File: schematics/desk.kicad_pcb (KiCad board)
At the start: 2 copper layers, 194 x 185 mm, 34 parts, among them K1 energized = UP (raises desk), K2 energized = DOWN (lowers desk), Q1 IRLZ44N, Q2 2N7000, Q3 2N7000, Q4 BC337, Q5 BC327, U1 LM2596HV 29V-5V, U2 PinSocket_1x22_P2.54mm_Vertic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, U3 74HC123 250ms, U5 ACS724xLCTR-05AB, U6 74HC08

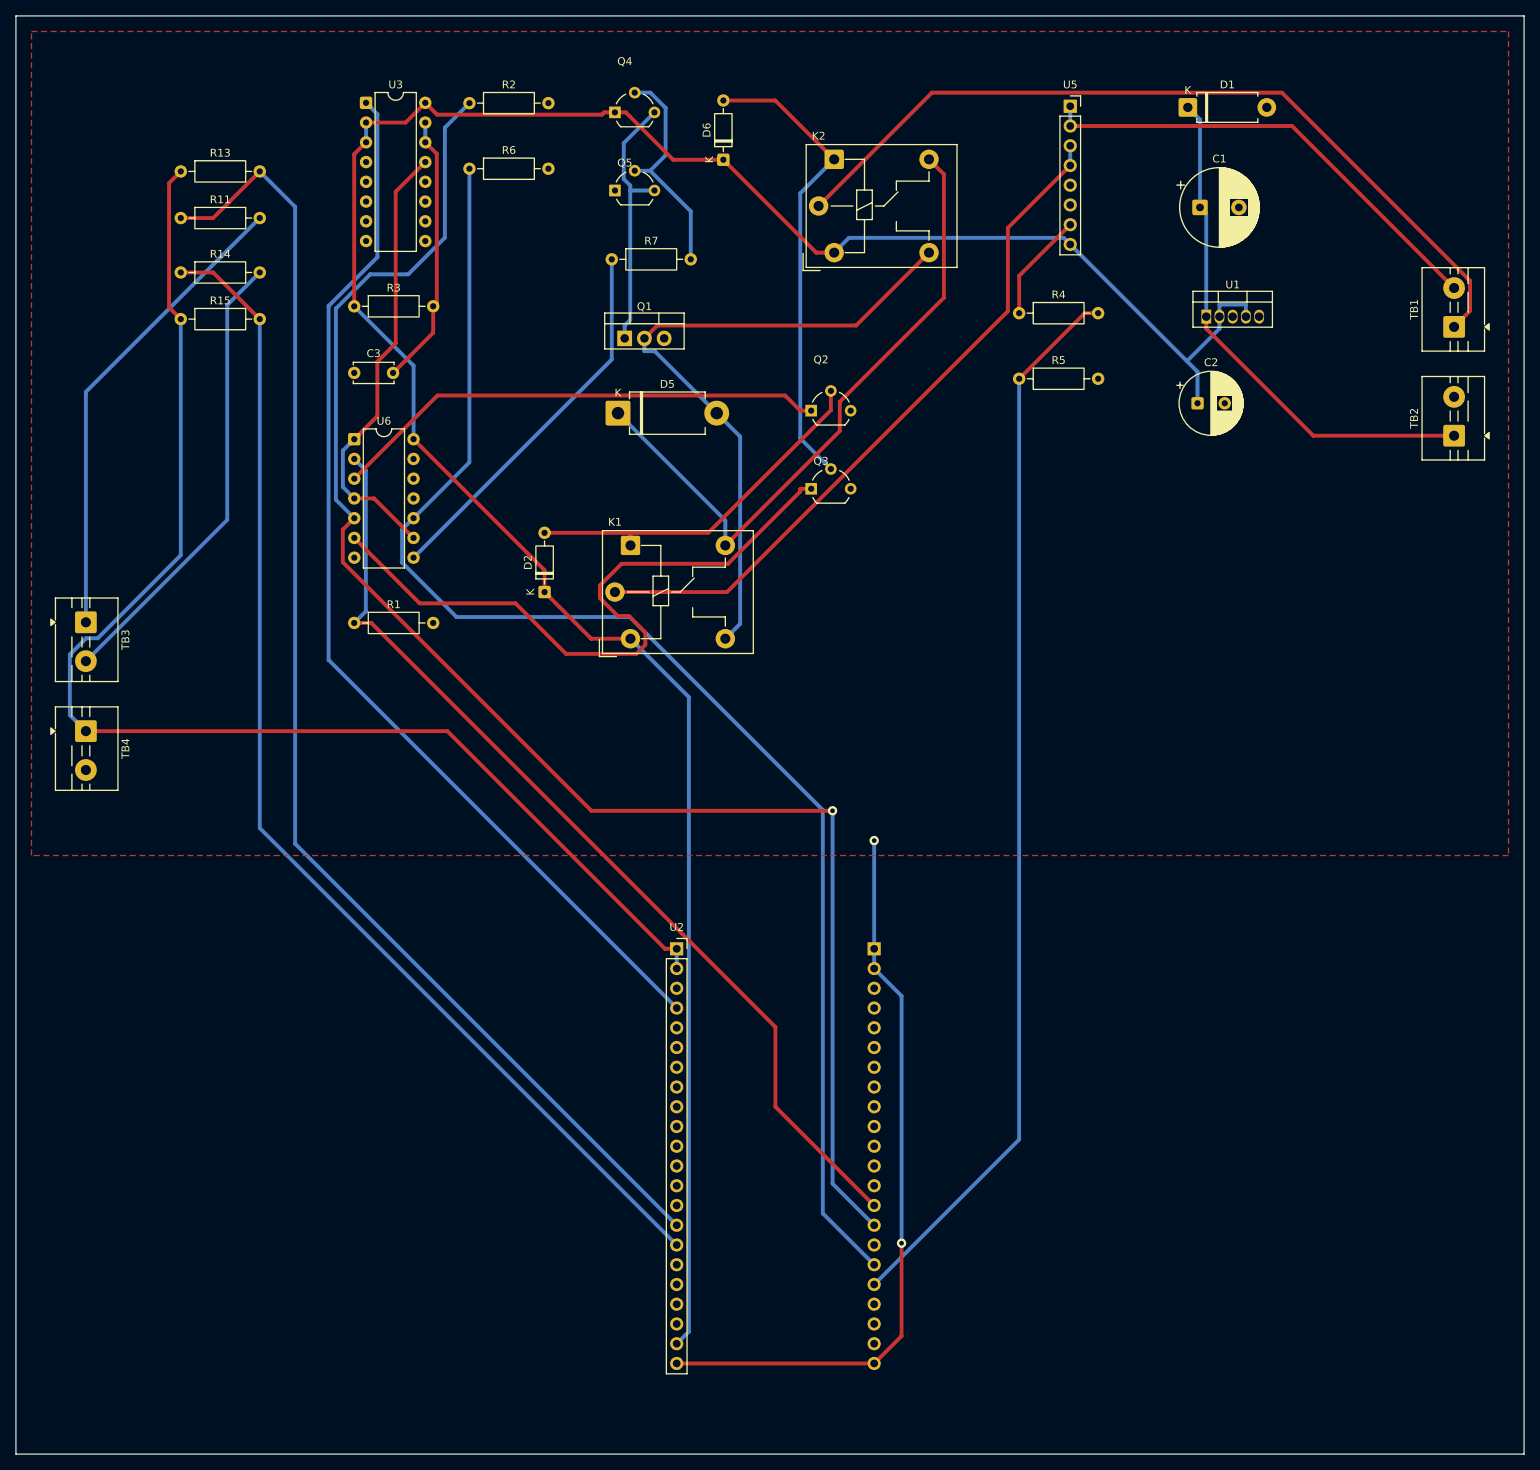
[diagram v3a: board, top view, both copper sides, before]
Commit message: Reposition U2 deliberately instead of tacking it onto a big new strip
The first on-board placement just expanded the board by 75mm and dropped
U2 in the middle of the new space with no reasoning behind where. Looked
at U2's actual connections: 7 of 10 signal groups (DIR_A/DIR_B/PWM/KICK/
SW_UP/SW_DN/+3V3) go to the logic cluster (U3/U6/rockers, x=9-55); only
ISENSE is purely power-side. Rotated U2 90 degrees (60.6mm wide x 39.4mm
tall instead of the other way around, cutting the needed board growth
roughly in half) and moved it under the logic cluster instead of
centering it in the new strip.

Board only needs to grow to 150mm tall now (was 185mm). Re-routed:
2 vias (was 3), 0 unconnected (was 1 minor GND-zone gap on D1), only one
cosmetic thermal-relief spoke-count warning left. Better in every way,
including the metric (via count) the placement change wasn't even
targeting.
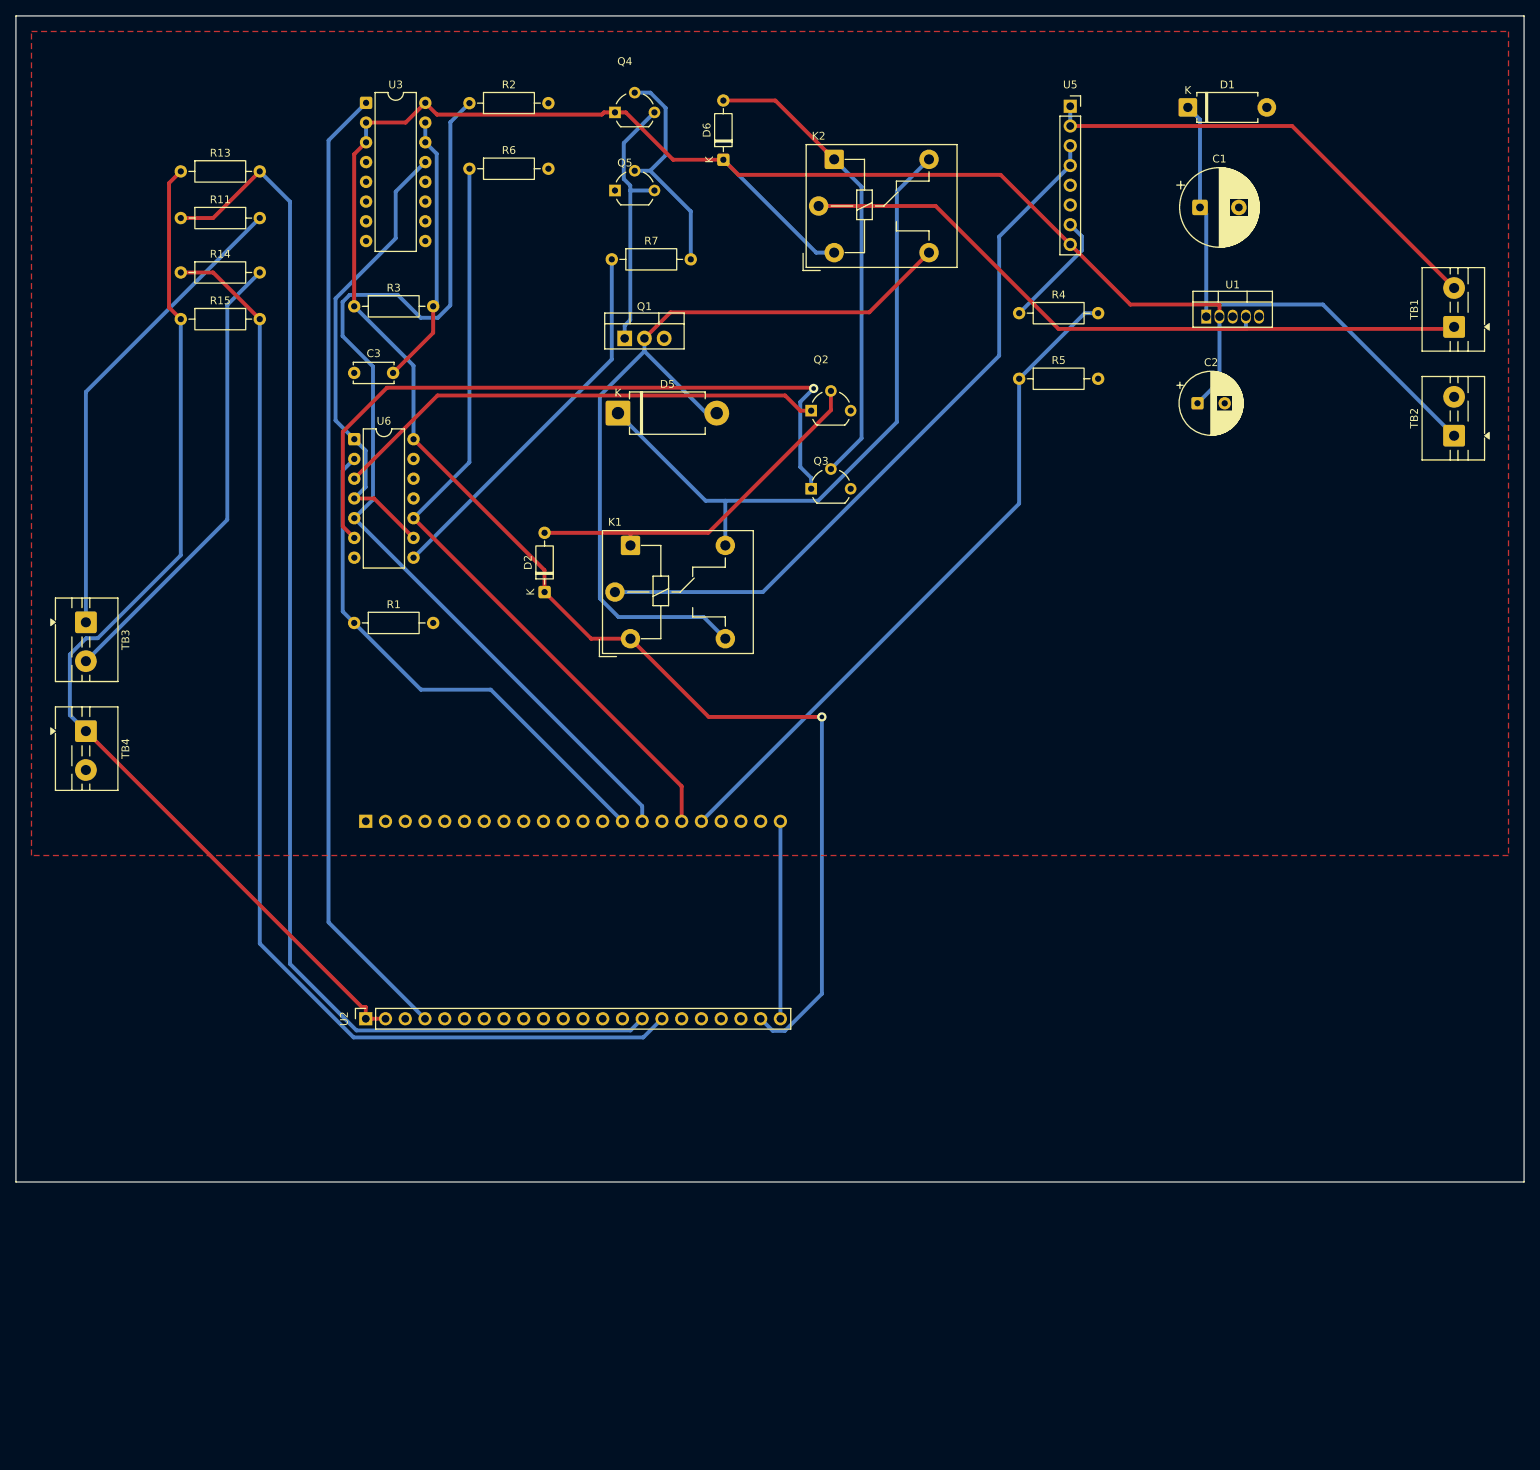
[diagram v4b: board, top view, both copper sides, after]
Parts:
- moved U2 41.0 mm to (45.0, 129.0), turned to 90 degrees
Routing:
- net PWM: track 182.8 -> 101.2 mm
- net DIR_B: track 202.4 -> 127.9 mm, vias 1 -> 0
- net GND: track 95.6 -> 25.4 mm, vias 2 -> 0
- net DIR_A: track 126.3 -> 67.4 mm
- net ISENSE: track 137.9 -> 87.5 mm
- net +3V3: track 171.0 -> 135.6 mm
- net /MRET: track 86.5 -> 107.9 mm
- net Net-(TB1-Pin_1): track 106.6 -> 88.4 mm
- net KICK: track 138.2 -> 125.0 mm
- net SW_UP: track 170.4 -> 165.7 mm
- net Net-(Q3-G): track 87.5 -> 91.4 mm, vias 0 -> 1
- net SW_DN: track 154.0 -> 150.7 mm
- net /DRV_UP: track 90.1 -> 92.8 mm
- net /WDOG: track 58.0 -> 60.0 mm
- net +5V: track 321.3 -> 319.4 mm, vias 0 -> 1
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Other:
- board size 194 x 185 mm -> 194 x 150 mm

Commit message: Re-route U2-onboard layout: 2 vias -> 0
Ran the placement optimizer (5mm displacement) then re-routed with
Freerouting instead of KiCadRoutingTools. Result routes fully on two
layers with zero through-connections needed. Also picked up the
missing B.Cu ground pour (GND_POUR_B), matching the F.Cu pour that
was already present.

0 unrouted, 0 unconnected, 0 real DRC violations. Remaining 8 DRC
items are cosmetic (silkscreen reference-field overlap, thermal-relief
spoke-count warnings on isolated pads) - same category of minor
warnings as prior committed states, not new.

A separate 30mm-displacement optimizer run was also tried; it moved
30 parts (crossings 82 -> 11) but bought no further via reduction
(already at the floor of 0) at the cost of more silkscreen clutter,
so it wasn't adopted.
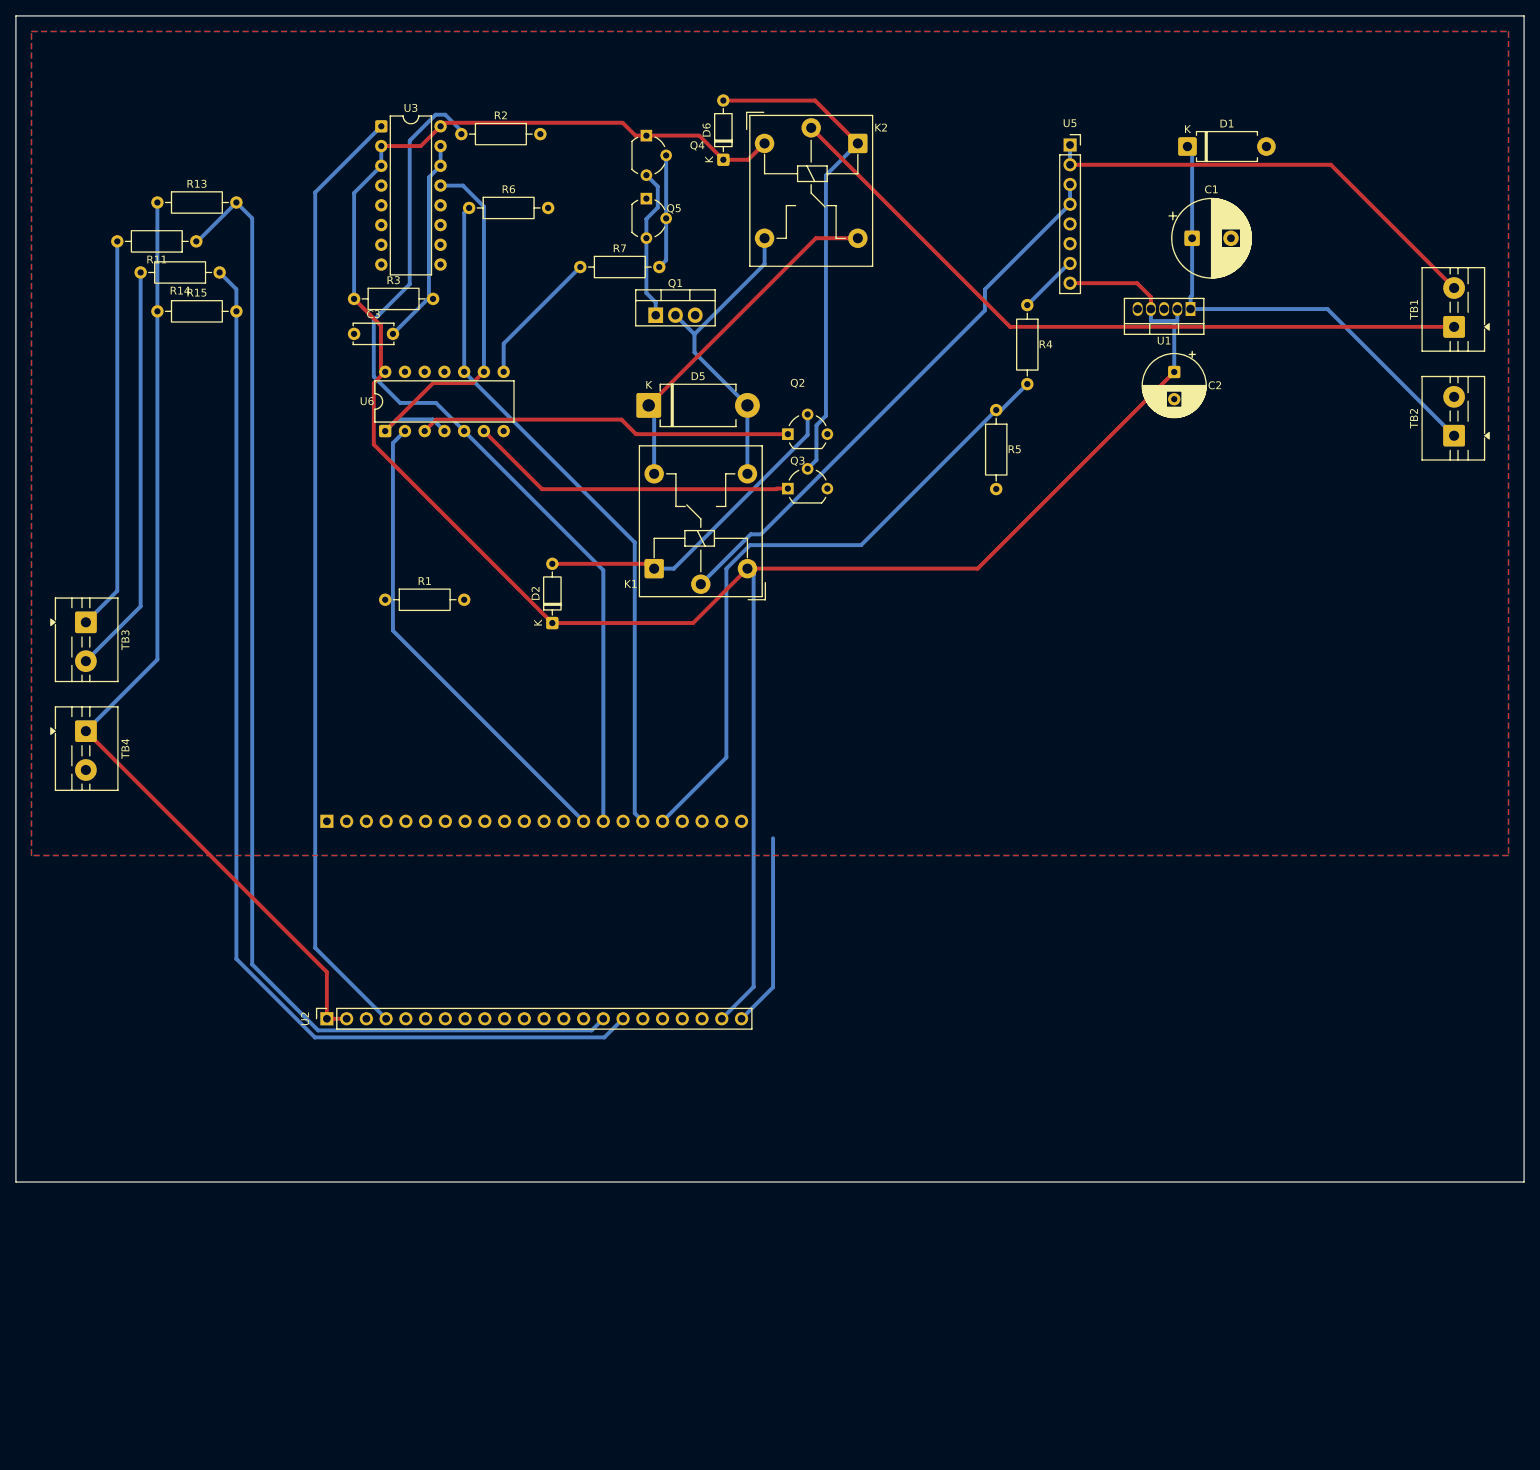
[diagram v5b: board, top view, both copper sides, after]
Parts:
- moved R6 5.05 mm to (58.3, 24.7)
- moved D1 5.03 mm to (150.7, 16.8)
- moved Q4 5.03 mm to (81.1, 15.4), turned to -90 degrees
- moved C3 5.02 mm to (43.5, 40.9)
- moved C2 5.02 mm to (149.0, 45.8), turned to -90 degrees
- moved R13 5.00 mm to (18.2, 24.0)
- moved U2 5.00 mm to (40.0, 129.0)
- moved R14 5.00 mm to (26.2, 33.0), turned to 180 degrees
- moved R5 4.99 mm to (126.1, 50.7), turned to -90 degrees
- moved U5 4.98 mm to (135.6, 16.6)
- moved Q1 4.98 mm to (82.3, 38.5)
- moved R1 4.98 mm to (47.5, 75.1)
- moved K1 4.27 mm to (82.1, 71.1), turned to 90 degrees
- moved Q2 4.26 mm to (99.3, 53.8)
- moved Q5 4.18 mm to (81.1, 23.5), turned to -90 degrees
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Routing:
- net /MRET: track 107.9 -> 40.3 mm
- net Net-(Q3-G): track 91.4 -> 42.2 mm, vias 1 -> 0
- net VSW: track 86.0 -> 44.9 mm
- net Net-(R7-Pad1): track 48.9 -> 17.6 mm
- net /DRV_UP: track 92.8 -> 71.9 mm
- net Net-(Q2-G): track 64.0 -> 48.1 mm
- net Net-(Q1-G): track 34.5 -> 19.7 mm
- net Net-(Q4-B): track 29.2 -> 14.7 mm
- net DIR_B: track 127.9 -> 113.7 mm
- net PWM: track 101.2 -> 88.7 mm
- net +5V: track 319.4 -> 307.0 mm, vias 1 -> 0
- net +3V3: track 135.6 -> 124.2 mm
- net Net-(TB3-Pin_1): track 61.3 -> 50.7 mm
- net SW_UP: track 165.7 -> 155.4 mm
- net Net-(U3A-Cext): track 35.1 -> 27.3 mm
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- added copper zone on B.Cu, net GND
